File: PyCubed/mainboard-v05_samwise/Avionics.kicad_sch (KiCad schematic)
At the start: 27 parts, among them SW1 KMR231NG LFS, U1 MAX706RESA, U2 ATSAMD51J20A-AU, Y1 32.768kHz

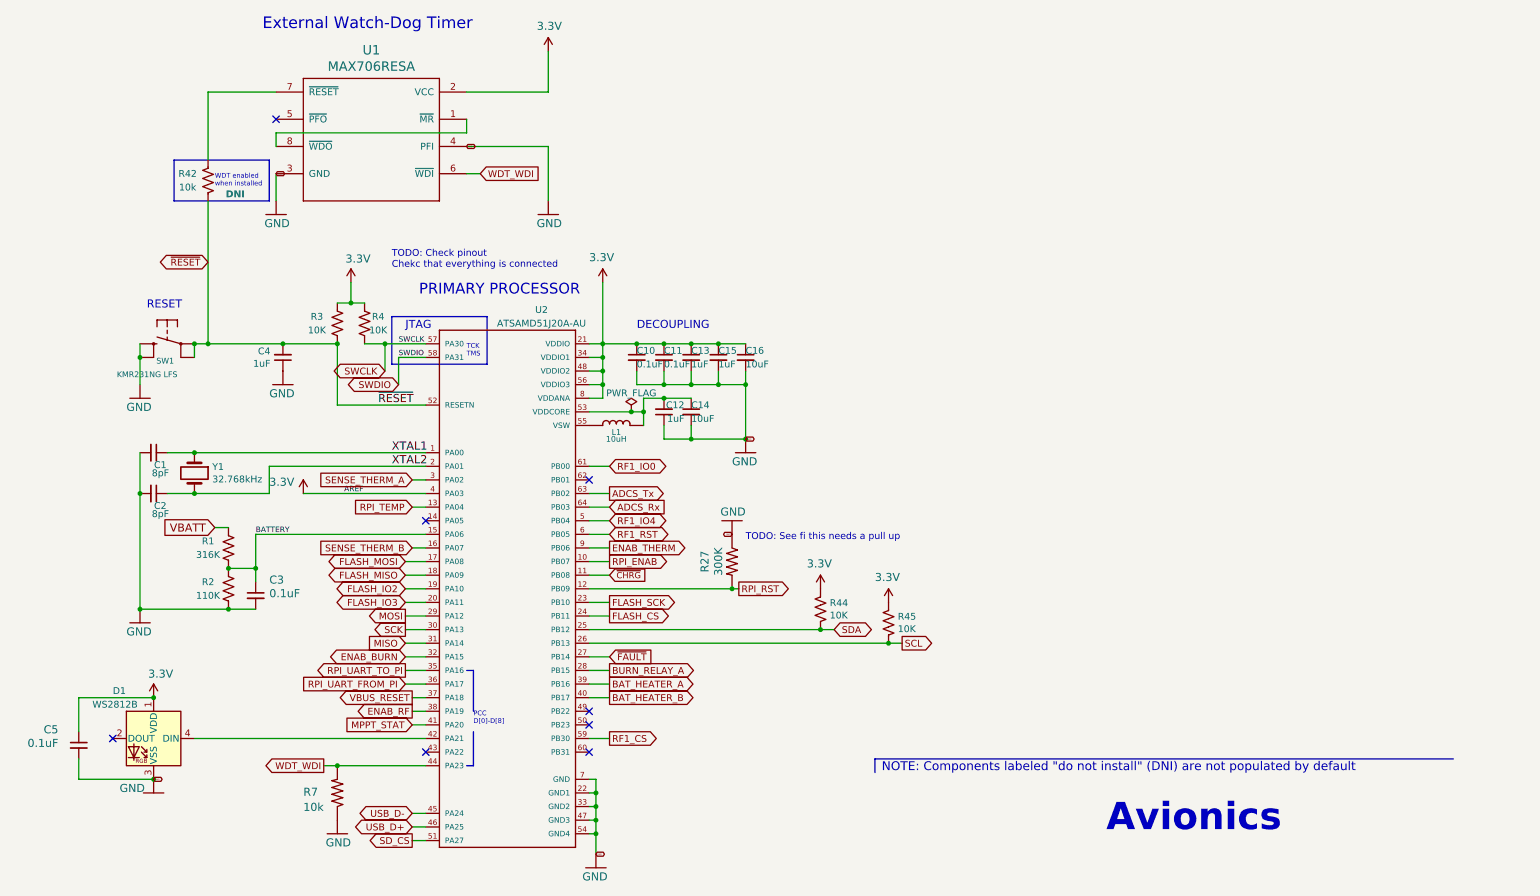
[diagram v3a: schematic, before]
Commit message: MPPT board connector added to Pycubed
This only changes the schematic. Footprint needs to be added.
Also resolved a conflict with IO resources between the MPPT circuit and the RGB LED
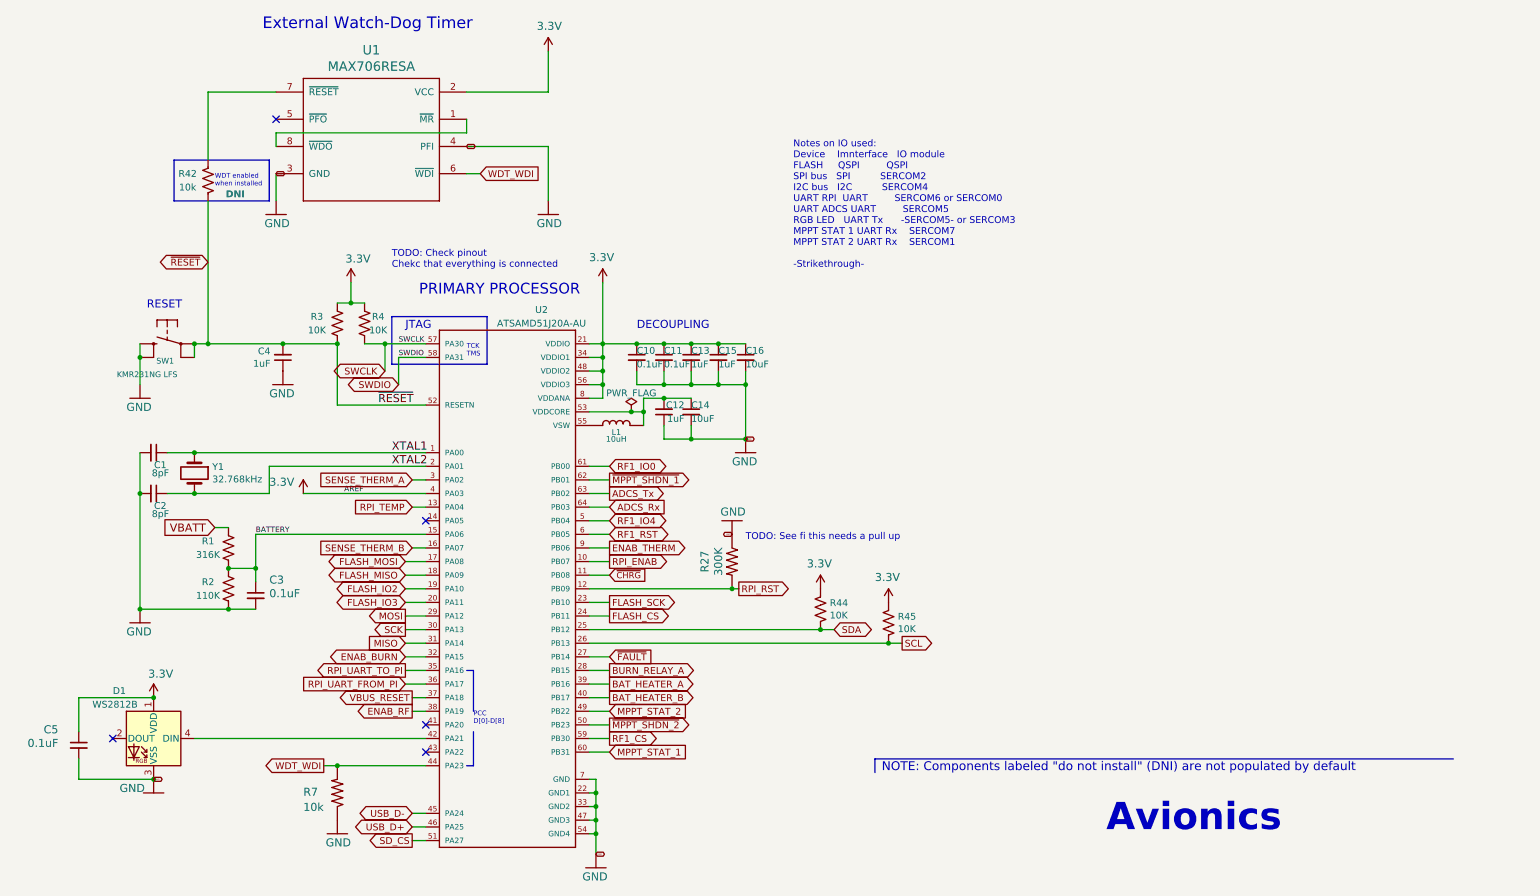
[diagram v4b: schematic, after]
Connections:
- net MPPT_STAT_2: now reaches U2.49 (PB22)
- net ~{MPPT_SHDN_2}: now reaches U2.50 (PB23)
- net MPPT_STAT_1: now reaches U2.60 (PB31)
- net ~{MPPT_SHDN_1}: now reaches U2.62 (PB01)
- net MPPT_STAT: no longer names the net of U2.41 (PA20)
- no-connect marks 8 -> 5
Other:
- note added: "Notes on IO used: Device Imnterface IO module FLASH QSPI QSPI SPI bus SPI SERCOM2 I2C bus I2C SERCOM4 UART RPI UART SERCOM6 or SERCOM0 UART ADCS UART SERCOM5 RGB LED UART Tx -SERCOM5- or SERCOM3 MPPT STAT 1 UART Rx SERCOM7 MPPT STAT 2 UART Rx SERCOM1 -Strikethrough-"
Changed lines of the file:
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@@
   (junction (at 137.16 85.09) (diameter 0) (color 0 0 0 0)
   )
-  (no_connect (at 123.19 110.49))
   (no_connect (at 92.71 161.29))
-  (no_connect (at 123.19 153.67))
   (no_connect (at 64.77 43.18))
-  (no_connect (at 123.19 161.29))
   (no_connect (at 34.29 158.75))
-  (no_connect (at 123.19 156.21))
+  (no_connect (at 92.71 156.21))
   (no_connect (at 92.71 118.11))
   (wire (pts (xy 78.74 77.47) (xy 81.28 77.47))
@@
     (stroke (width 0) (type default))
   )
+  (wire (pts (xy 123.19 156.21) (xy 127 156.21))
+    (stroke (width 0) (type default))
+  )
   (wire (pts (xy 90.17 151.13) (xy 92.71 151.13))
     (stroke (width 0) (type default))
@@
     (stroke (width 0) (type default))
   )
+  (wire (pts (xy 123.19 161.29) (xy 127 161.29))
+    (stroke (width 0) (type default))
+  )
   (wire (pts (xy 133.35 97.79) (xy 133.35 95.25))
     (stroke (width 0) (type default))
@@
     (stroke (width 0) (type default))
   )
+  (wire (pts (xy 123.19 153.67) (xy 127 153.67))
+    (stroke (width 0) (type default))
+  )
   (polyline (pts (xy 100.33 146.05) (xy 101.6 146.05))
     (stroke (width 0) (type default))
@@
     (stroke (width 0) (type default))
   )
-  (wire (pts (xy 90.17 156.21) (xy 92.71 156.21))
-    (stroke (width 0) (type default))
-  )
   (wire (pts (xy 64.77 38.1) (xy 52.07 38.1))
     (stroke (width 0) (type default))
@@
   )
   (wire (pts (xy 137.16 92.71) (xy 132.08 92.71))
+    (stroke (width 0) (type default))
+  )
+  (wire (pts (xy 123.19 110.49) (xy 127 110.49))
     (stroke (width 0) (type default))
   )
@@
   (text "TCK\nTMS" (at 100.33 87.63 0)
     (effects (font (size 0.889 0.889)) (justify left bottom))
+  )
+  (text "Notes on IO used:\nDevice    Imnterface   IO module\nFLASH     QSPI         QSPI\nSPI bus   SPI          SERCOM2\nI2C bus   I2C          SERCOM4\nUART RPI  UART         SERCOM6 or SERCOM0\nUART ADCS UART         SERCOM5\nRGB LED   UART Tx      -SERCOM5- or SERCOM3\nMPPT STAT 1 UART Rx    SERCOM7\nMPPT STAT 2 UART Rx    SERCOM1\n\n-Strikethrough-"
+    (at 161.29 71.12 0)
+    (effects (font (size 1.27 1.27)) (justify left bottom))
   )
   (text "RESET" (at 40.64 78.74 0)
@@
     )
   )
+  (global_label "~{MPPT_SHDN_1}" (shape output) (at 127 110.49 0) (fields_autoplaced)
+    (effects (font (size 1.27 1.27)) (justify left))
+    (property "Intersheetrefs" "${INTERSHEET_REFS}" (at 142.5752 110.49 0)
+      (effects (font (size 1.27 1.27)) (justify left) hide)
+    )
+  )
   (global_label "GND" (shape bidirectional) (at 64.77 53.34 0) (fields_autoplaced)
     (effects (font (size 0.254 0.254)) (justify left))
@@
     )
   )
+  (global_label "MPPT_STAT_1" (shape input) (at 127 161.29 0) (fields_autoplaced)
+    (effects (font (size 1.27 1.27)) (justify left))
+    (property "Intersheetrefs" "${INTERSHEET_REFS}" (at 141.668 161.29 0)
+      (effects (font (size 1.27 1.27)) (justify left) hide)
+    )
+  )
   (global_label "WDT_WDI" (shape output) (at 73.66 163.83 180) (fields_autoplaced)
     (effects (font (size 1.27 1.27)) (justify right))
     (property "Intersheetrefs" "${INTERSHEET_REFS}" (at 63.4256 163.83 0)
-      (effects (font (size 1.27 1.27)) (justify right) hide)
-    )
-  )
-  (global_label "MPPT_STAT" (shape input) (at 90.17 156.21 180) (fields_autoplaced)
-    (effects (font (size 1.27 1.27)) (justify right))
-    (property "Intersheetrefs" "${INTERSHEET_REFS}" (at 77.6791 156.21 0)
       (effects (font (size 1.27 1.27)) (justify right) hide)
     )
@@
     )
   )
+  (global_label "~{MPPT_SHDN_2}" (shape output) (at 127 156.21 0) (fields_autoplaced)
+    (effects (font (size 1.27 1.27)) (justify left))
+    (property "Intersheetrefs" "${INTERSHEET_REFS}" (at 142.5752 156.21 0)
+      (effects (font (size 1.27 1.27)) (justify left) hide)
+    )
+  )
   (global_label "SWCLK" (shape bidirectional) (at 85.09 90.17 180) (fields_autoplaced)
     (effects (font (size 1.27 1.27)) (justify right))
@@
     )
   )
+  (global_label "MPPT_STAT_2" (shape input) (at 127 153.67 0) (fields_autoplaced)
+    (effects (font (size 1.27 1.27)) (justify left))
+    (property "Intersheetrefs" "${INTERSHEET_REFS}" (at 141.668 153.67 0)
+      (effects (font (size 1.27 1.27)) (justify left) hide)
+    )
+  )

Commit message: Layout and Routing work
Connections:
- net ENAB_RF: now also U2.6 (PB05); no longer U2.38 (PA19)
- net RF1_RST: now also U2.38 (PA19); no longer U2.6 (PB05)
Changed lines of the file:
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@@
+    (stroke (width 0) (type default))
+  )
+  (wire (pts (xy 123.19 120.65) (xy 127 120.65))
     (stroke (width 0) (type default))
   )
@@
     (stroke (width 0) (type default))
   )
+  (wire (pts (xy 90.17 153.67) (xy 92.71 153.67))
+    (stroke (width 0) (type default))
+  )
   (wire (pts (xy 27.94 166.37) (xy 41.91 166.37))
     (stroke (width 0) (type default))
@@
     (stroke (width 0) (type default))
   )
-  (wire (pts (xy 127 120.65) (xy 123.19 120.65))
-    (stroke (width 0) (type default))
-  )
   (wire (pts (xy 49.53 113.03) (xy 63.5 113.03))
     (stroke (width 0) (type default))
@@
   )
   (wire (pts (xy 123.19 173.99) (xy 124.46 173.99))
-    (stroke (width 0) (type default))
-  )
-  (wire (pts (xy 92.71 153.67) (xy 90.17 153.67))
     (stroke (width 0) (type default))
   )
@@
     )
   )
-  (global_label "ENAB_RF" (shape output) (at 90.17 153.67 180) (fields_autoplaced)
-    (effects (font (size 1.27 1.27)) (justify right))
-    (property "Intersheetrefs" "${INTERSHEET_REFS}" (at 79.6747 153.67 0)
-      (effects (font (size 1.27 1.27)) (justify right) hide)
+  (global_label "ENAB_RF" (shape output) (at 127 120.65 0) (fields_autoplaced)
+    (effects (font (size 1.27 1.27)) (justify left))
+    (property "Intersheetrefs" "${INTERSHEET_REFS}" (at 137.4953 120.65 0)
+      (effects (font (size 1.27 1.27)) (justify left) hide)
     )
   )
@@
     )
   )
-  (global_label "RF1_RST" (shape bidirectional) (at 127 120.65 0) (fields_autoplaced)
-    (effects (font (size 1.27 1.27)) (justify left))
-    (property "Intersheetrefs" "${INTERSHEET_REFS}" (at 137.3071 120.5706 0)
-      (effects (font (size 1.27 1.27)) (justify left) hide)
-    )
-  )
+  (global_label "RF1_RST" (shape bidirectional) (at 90.17 153.67 180) (fields_autoplaced)
+    (effects (font (size 1.27 1.27)) (justify right))
+    (property "Intersheetrefs" "${INTERSHEET_REFS}" (at 78.9037 153.67 0)
+      (effects (font (size 1.27 1.27)) (justify right) hide)
+    )
+  )

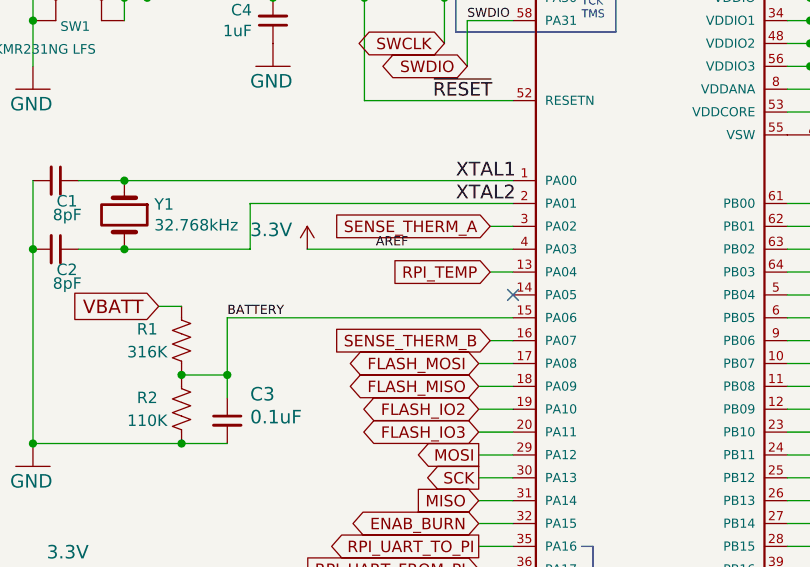
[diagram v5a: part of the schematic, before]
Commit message: Everything is connected
Also no clearance violations
Still some courtyard overlaps that should not mater
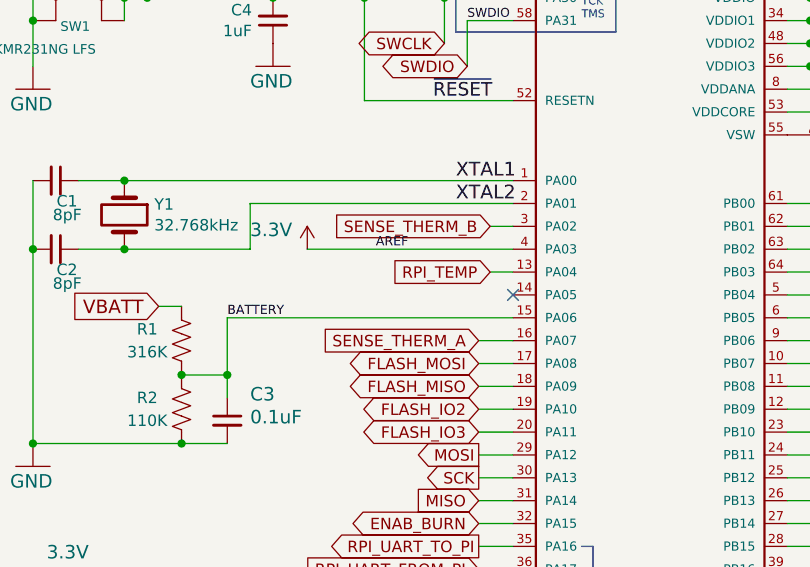
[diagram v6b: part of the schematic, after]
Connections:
- net SENSE_THERM_A: now also U2.16 (PA07); no longer U2.3 (PA02)
- net SENSE_THERM_B: now also U2.3 (PA02); no longer U2.16 (PA07)
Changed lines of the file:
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@@
-    (stroke (width 0) (type default))
-  )
-  (wire (pts (xy 92.71 110.49) (xy 90.17 110.49))
     (stroke (width 0) (type default))
   )
@@
     (stroke (width 0) (type default))
   )
+  (wire (pts (xy 90.17 110.49) (xy 92.71 110.49))
+    (stroke (width 0) (type default))
+  )
   (wire (pts (xy 115.57 38.1) (xy 100.33 38.1))
     (stroke (width 0) (type default))
@@
     (stroke (width 0) (type default))
   )
+  (wire (pts (xy 88.9 123.19) (xy 92.71 123.19))
+    (stroke (width 0) (type default))
+  )
   (wire (pts (xy 133.35 97.79) (xy 133.35 95.25))
     (stroke (width 0) (type default))
@@
   )
   (wire (pts (xy 142.24 92.71) (xy 137.16 92.71))
-    (stroke (width 0) (type default))
-  )
-  (wire (pts (xy 92.71 123.19) (xy 90.17 123.19))
     (stroke (width 0) (type default))
   )
@@
     )
   )
-  (global_label "SENSE_THERM_B" (shape input) (at 90.17 123.19 180) (fields_autoplaced)
-    (effects (font (size 1.27 1.27)) (justify right))
-    (property "Intersheetrefs" "${INTERSHEET_REFS}" (at 72.4178 123.19 0)
+  (global_label "SENSE_THERM_B" (shape input) (at 90.17 110.49 180) (fields_autoplaced)
+    (effects (font (size 1.27 1.27)) (justify right))
+    (property "Intersheetrefs" "${INTERSHEET_REFS}" (at 72.4178 110.49 0)
       (effects (font (size 1.27 1.27)) (justify right) hide)
     )
@@
     )
   )
-  (global_label "SENSE_THERM_A" (shape input) (at 90.17 110.49 180) (fields_autoplaced)
-    (effects (font (size 1.27 1.27)) (justify right))
-    (property "Intersheetrefs" "${INTERSHEET_REFS}" (at 72.5992 110.49 0)
-      (effects (font (size 1.27 1.27)) (justify right) hide)
-    )
+  (global_label "SENSE_THERM_A" (shape input) (at 88.9 123.19 180) (fields_autoplaced)
+    (effects (font (size 1.27 1.27)) (justify right))
+    (property "Intersheetrefs" "${INTERSHEET_REFS}" (at 71.3292 123.19 0)
+      (effects (font (size 1.27 1.27)) (justify right) hide)
+    )

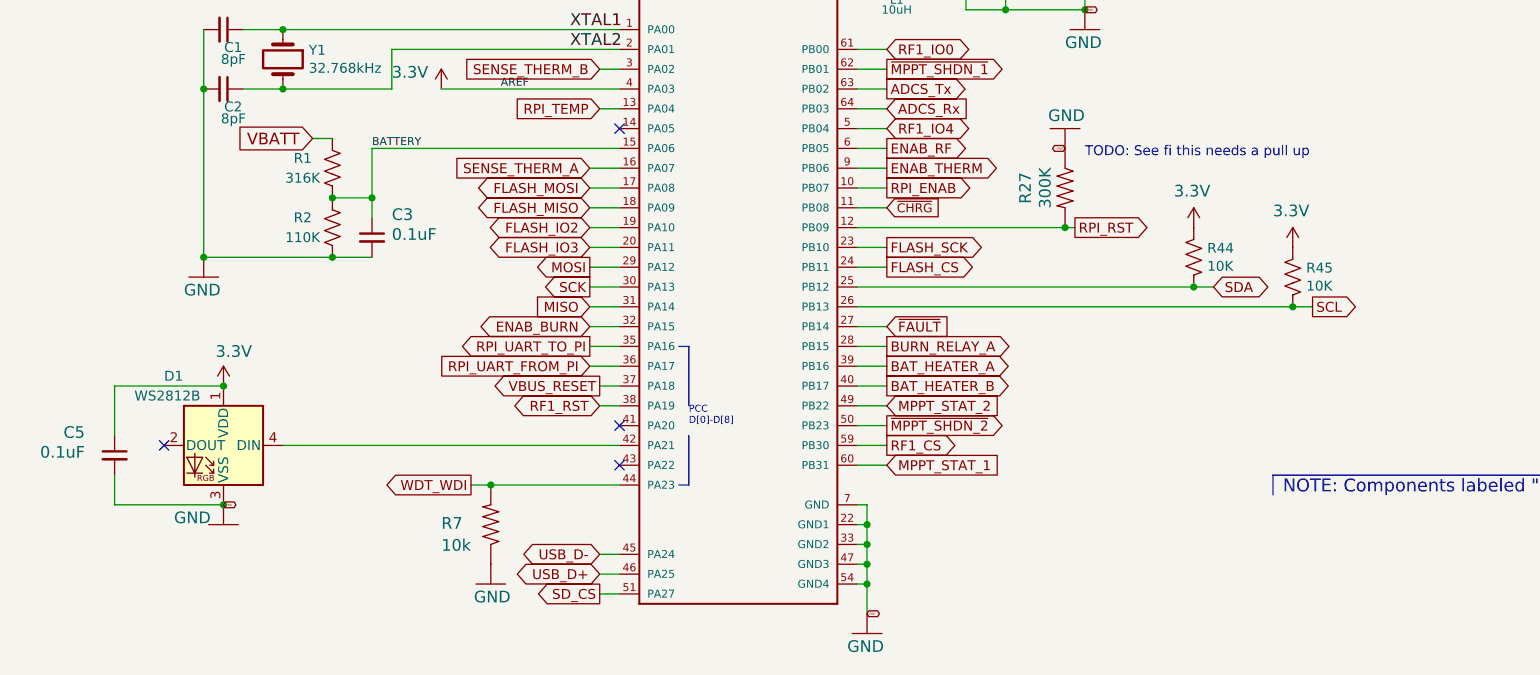
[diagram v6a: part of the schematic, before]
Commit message: some silkscreen edits
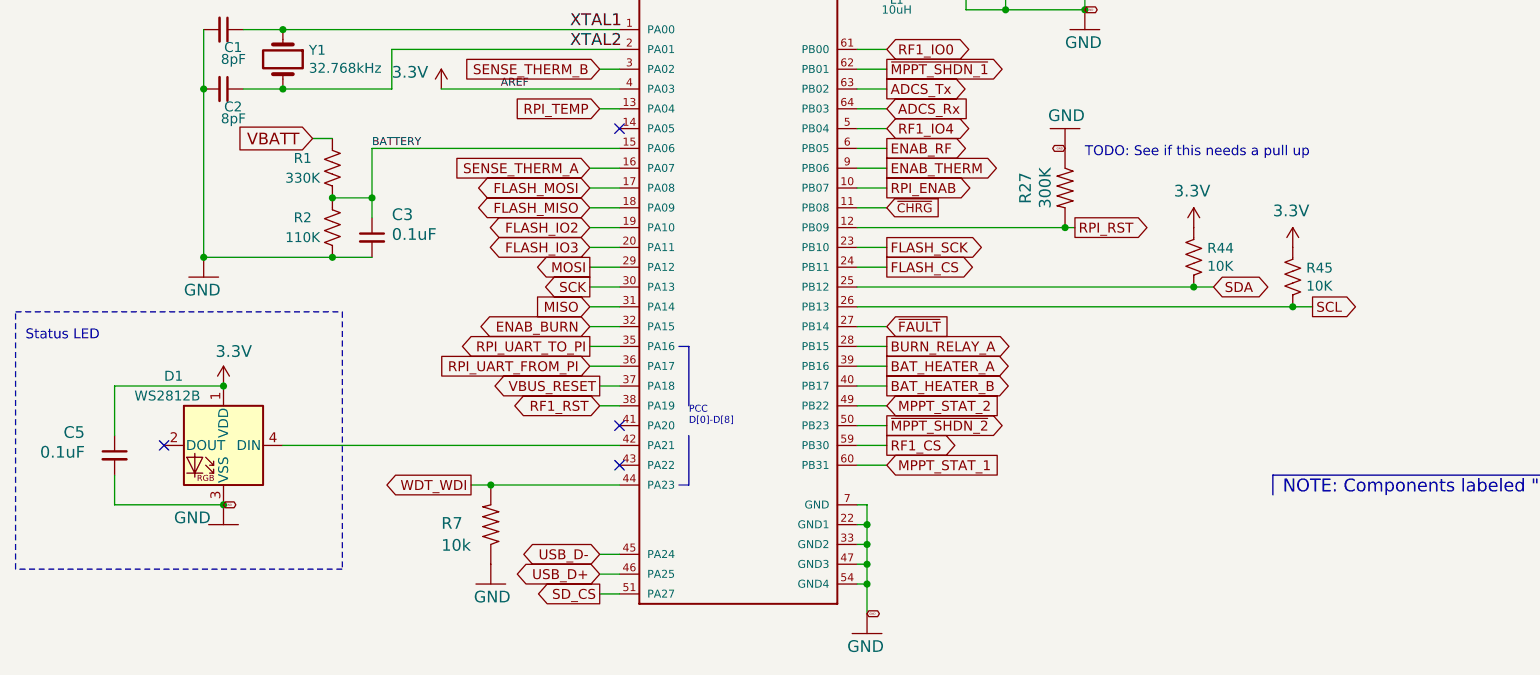
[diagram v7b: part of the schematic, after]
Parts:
- R1: value 316K -> 330K
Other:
- note added: "Status LED"
- note added: "TODO: See if this needs a pull up"
- note removed: "TODO: See fi this needs a pull up"
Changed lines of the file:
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@@
     (stroke (width 0) (type default))
+  )
+  (rectangle (start 15.24 141.605) (end 57.15 174.625)
+    (stroke (width 0) (type dash))
+    (fill (type none))
   )
   (text "PRIMARY PROCESSOR" (at 91.44 76.2 0)
@@
     (effects (font (size 1.27 1.27) (color 255 2 0 1)) (justify left bottom))
   )
-  (text "TODO: See fi this needs a pull up" (at 152.4 121.92 0)
+  (text "TODO: See if this needs a pull up" (at 152.4 121.92 0)
     (effects (font (size 1.27 1.27) (color 255 2 0 1)) (justify left bottom))
+  )
+  (text "Status LED" (at 16.51 145.415 0)
+    (effects (font (size 1.27 1.27)) (justify left bottom))
   )
   (text "External Watch-Dog Timer" (at 62.23 26.67 0)
@@
       (effects (font (size 1.27 1.27)))
     )
-    (property "Value" "316K" (at 52.07 124.46 0)
+    (property "Value" "330K" (at 52.07 124.46 0)
       (effects (font (size 1.27 1.27)))
     )
